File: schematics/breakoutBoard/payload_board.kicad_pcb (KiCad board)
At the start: 4 copper layers, 75 x 107 mm, 23 parts, among them P1 CONN_02X50, P2 CONN_02X50, P3 CONN_02X50, P4 CONN_02X50, U1 CBP, U2 TAMP, U3 CBP, U4 TAMP, U5 LAT-3, U6 TAMP

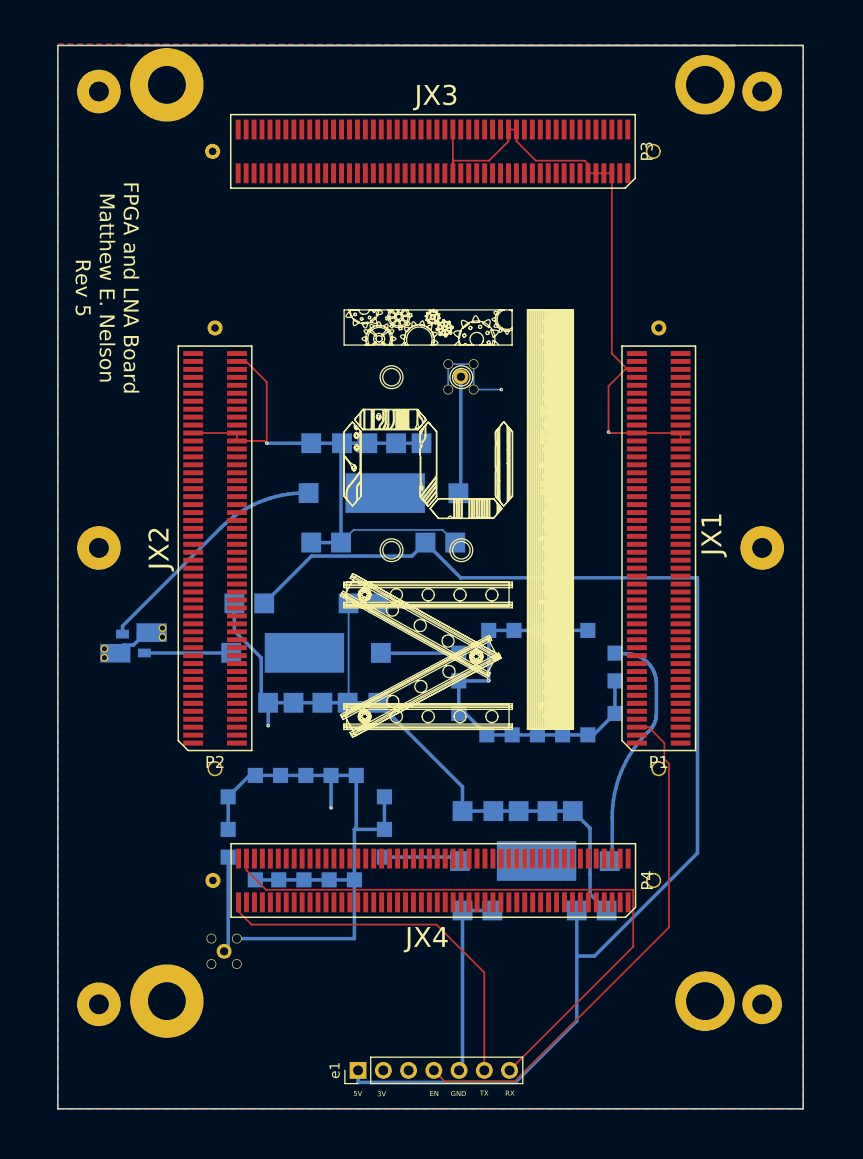
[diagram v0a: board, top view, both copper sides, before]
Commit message: Updated board to KiCad 6, pushing previous changes made.
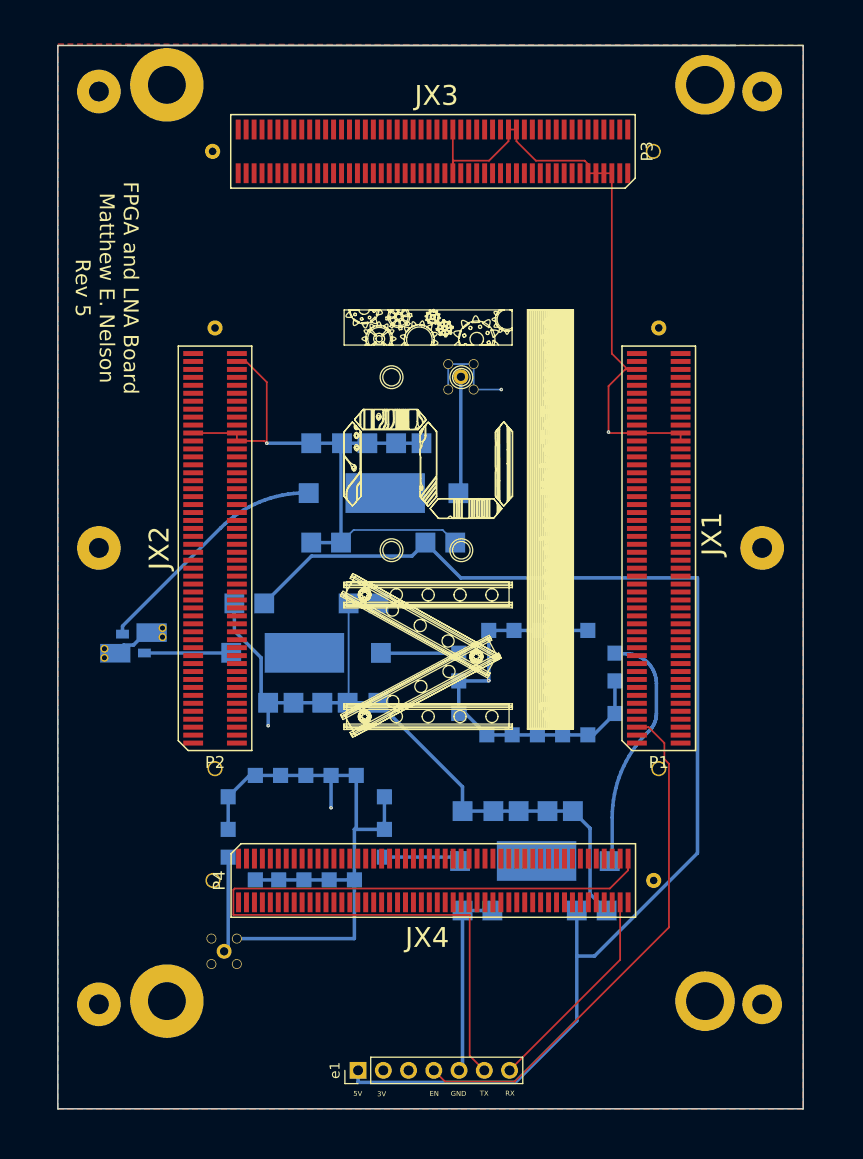
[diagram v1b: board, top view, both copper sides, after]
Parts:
- turned P4 to 0 degrees
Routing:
- net TX: track 38.0 -> 84.3 mm
- net RX: track 64.2 -> 21.5 mm
- net Net-(U5-Pad2): track 25.8 -> 24.8 mm
- net GND: track 218.7 -> 217.7 mm
- net Net-(U2-Pad5): track 25.7 -> 25.0 mm
- net RF_SIG: track 10.3 -> 9.65 mm
- added copper zone on In1.Cu, net GND
- added copper zone on In2.Cu, net RFGND
- removed copper zone on PGND, net GND
- removed copper zone on RFGND, net RFGND
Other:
- net class Default removed

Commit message: Update
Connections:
- net RF_SIG renamed /LNA Side/RF_SIG
- P1 pad 1: (no net) -> unconnected-(P1-Pad1)
- P1 pad 10: (no net) -> unconnected-(P1-Pad10)
- P1 pad 100: (no net) -> unconnected-(P1-Pad100)
- P1 pad 11: (no net) -> unconnected-(P1-Pad11)
- P1 pad 12: (no net) -> unconnected-(P1-Pad12)
- P1 pad 13: (no net) -> unconnected-(P1-Pad13)
- P1 pad 14: (no net) -> unconnected-(P1-Pad14)
- P1 pad 15: (no net) -> GND
- P1 pad 16: (no net) -> GND
- P1 pad 17: (no net) -> unconnected-(P1-Pad17)
- P1 pad 18: (no net) -> unconnected-(P1-Pad18)
- P1 pad 19: (no net) -> unconnected-(P1-Pad19)
- P1 pad 2: (no net) -> unconnected-(P1-Pad2)
- P1 pad 20: (no net) -> unconnected-(P1-Pad20)
- P1 pad 21: (no net) -> GND
- P1 pad 22: (no net) -> GND
- P1 pad 23: (no net) -> unconnected-(P1-Pad23)
- P1 pad 24: (no net) -> unconnected-(P1-Pad24)
- P1 pad 25: (no net) -> unconnected-(P1-Pad25)
- P1 pad 26: (no net) -> unconnected-(P1-Pad26)
- P1 pad 27: (no net) -> GND
- P1 pad 28: (no net) -> GND
- P1 pad 29: (no net) -> unconnected-(P1-Pad29)
- P1 pad 3: (no net) -> unconnected-(P1-Pad3)
- P1 pad 30: (no net) -> unconnected-(P1-Pad30)
- P1 pad 31: (no net) -> unconnected-(P1-Pad31)
- P1 pad 32: (no net) -> unconnected-(P1-Pad32)
- P1 pad 33: (no net) -> GND
- P1 pad 34: (no net) -> GND
- P1 pad 35: (no net) -> unconnected-(P1-Pad35)
- P1 pad 36: (no net) -> unconnected-(P1-Pad36)
- P1 pad 37: (no net) -> unconnected-(P1-Pad37)
- P1 pad 38: (no net) -> unconnected-(P1-Pad38)
- P1 pad 39: (no net) -> GND
- P1 pad 4: (no net) -> unconnected-(P1-Pad4)
- P1 pad 40: (no net) -> GND
- P1 pad 41: (no net) -> unconnected-(P1-Pad41)
- P1 pad 42: (no net) -> unconnected-(P1-Pad42)
- P1 pad 43: (no net) -> unconnected-(P1-Pad43)
- P1 pad 44: (no net) -> unconnected-(P1-Pad44)
- P1 pad 45: (no net) -> GND
- P1 pad 46: (no net) -> GND
- P1 pad 47: (no net) -> unconnected-(P1-Pad47)
- P1 pad 48: (no net) -> unconnected-(P1-Pad48)
- P1 pad 49: (no net) -> unconnected-(P1-Pad49)
- P1 pad 50: (no net) -> unconnected-(P1-Pad50)
- P1 pad 51: (no net) -> GND
- P1 pad 52: (no net) -> GND
- P1 pad 53: (no net) -> unconnected-(P1-Pad53)
- P1 pad 54: (no net) -> unconnected-(P1-Pad54)
- P1 pad 55: (no net) -> unconnected-(P1-Pad55)
- P1 pad 56: (no net) -> unconnected-(P1-Pad56)
- P1 pad 57: 3V -> 5V
- P1 pad 58: 3V -> 5V
- P1 pad 59: 3V -> 5V
- P1 pad 6: (no net) -> unconnected-(P1-Pad6)
- P1 pad 60: 3V -> 5V
- P1 pad 61: (no net) -> unconnected-(P1-Pad61)
- P1 pad 62: (no net) -> unconnected-(P1-Pad62)
- P1 pad 63: (no net) -> unconnected-(P1-Pad63)
- P1 pad 64: (no net) -> unconnected-(P1-Pad64)
- P1 pad 65: (no net) -> GND
- P1 pad 66: (no net) -> GND
- P1 pad 67: (no net) -> unconnected-(P1-Pad67)
- P1 pad 68: (no net) -> unconnected-(P1-Pad68)
- P1 pad 69: (no net) -> unconnected-(P1-Pad69)
- P1 pad 7: (no net) -> GND
- P1 pad 70: (no net) -> unconnected-(P1-Pad70)
- P1 pad 71: (no net) -> GND
- P1 pad 72: (no net) -> GND
- P1 pad 73: (no net) -> unconnected-(P1-Pad73)
- P1 pad 74: (no net) -> unconnected-(P1-Pad74)
- P1 pad 75: (no net) -> unconnected-(P1-Pad75)
- P1 pad 76: (no net) -> unconnected-(P1-Pad76)
- P1 pad 77: (no net) -> GND
- P1 pad 8: (no net) -> unconnected-(P1-Pad8)
- P1 pad 81: (no net) -> unconnected-(P1-Pad81)
- P1 pad 82: (no net) -> unconnected-(P1-Pad82)
- P1 pad 83: (no net) -> unconnected-(P1-Pad83)
- P1 pad 84: (no net) -> unconnected-(P1-Pad84)
- P1 pad 85: (no net) -> GND
- P1 pad 86: (no net) -> GND
- P1 pad 87: (no net) -> unconnected-(P1-Pad87)
- P1 pad 88: (no net) -> unconnected-(P1-Pad88)
- P1 pad 89: (no net) -> unconnected-(P1-Pad89)
- P1 pad 9: (no net) -> unconnected-(P1-Pad9)
- P1 pad 90: (no net) -> unconnected-(P1-Pad90)
- P1 pad 91: (no net) -> unconnected-(P1-Pad91)
- P1 pad 92: (no net) -> unconnected-(P1-Pad92)
- P1 pad 93: (no net) -> unconnected-(P1-Pad93)
- P1 pad 94: (no net) -> unconnected-(P1-Pad94)
- P1 pad 96: (no net) -> GND
- P1 pad 97: (no net) -> unconnected-(P1-Pad97)
- P1 pad 98: (no net) -> unconnected-(P1-Pad98)
- P1 pad 99: (no net) -> unconnected-(P1-Pad99)
- P2 pad 1: (no net) -> unconnected-(P2-Pad1)
- P2 pad 10: (no net) -> unconnected-(P2-Pad10)
- P2 pad 100: (no net) -> unconnected-(P2-Pad100)
- P2 pad 11: (no net) -> unconnected-(P2-Pad11)
- P2 pad 12: 3V -> 5V
- P2 pad 13: (no net) -> unconnected-(P2-Pad13)
- P2 pad 14: (no net) -> unconnected-(P2-Pad14)
- P2 pad 15: (no net) -> GND
- P2 pad 16: (no net) -> GND
- P2 pad 17: (no net) -> unconnected-(P2-Pad17)
- P2 pad 18: (no net) -> unconnected-(P2-Pad18)
- P2 pad 19: (no net) -> unconnected-(P2-Pad19)
- P2 pad 2: (no net) -> unconnected-(P2-Pad2)
- P2 pad 20: (no net) -> unconnected-(P2-Pad20)
- P2 pad 21: (no net) -> GND
- P2 pad 22: (no net) -> GND
- P2 pad 23: (no net) -> unconnected-(P2-Pad23)
- P2 pad 24: (no net) -> unconnected-(P2-Pad24)
- P2 pad 25: (no net) -> unconnected-(P2-Pad25)
- P2 pad 26: (no net) -> unconnected-(P2-Pad26)
- P2 pad 27: (no net) -> GND
- P2 pad 28: (no net) -> GND
- P2 pad 29: (no net) -> unconnected-(P2-Pad29)
- P2 pad 3: (no net) -> unconnected-(P2-Pad3)
- P2 pad 30: (no net) -> unconnected-(P2-Pad30)
- P2 pad 31: (no net) -> unconnected-(P2-Pad31)
- P2 pad 32: (no net) -> unconnected-(P2-Pad32)
- P2 pad 33: (no net) -> GND
- P2 pad 34: (no net) -> GND
- P2 pad 35: (no net) -> unconnected-(P2-Pad35)
- P2 pad 36: (no net) -> unconnected-(P2-Pad36)
- P2 pad 37: (no net) -> unconnected-(P2-Pad37)
- P2 pad 38: (no net) -> unconnected-(P2-Pad38)
- P2 pad 39: (no net) -> GND
- P2 pad 4: (no net) -> unconnected-(P2-Pad4)
- P2 pad 40: (no net) -> GND
- P2 pad 41: (no net) -> unconnected-(P2-Pad41)
- P2 pad 42: (no net) -> unconnected-(P2-Pad42)
- P2 pad 43: (no net) -> unconnected-(P2-Pad43)
- P2 pad 44: (no net) -> unconnected-(P2-Pad44)
- P2 pad 45: (no net) -> GND
- P2 pad 46: (no net) -> GND
- P2 pad 47: (no net) -> unconnected-(P2-Pad47)
- P2 pad 48: (no net) -> unconnected-(P2-Pad48)
- P2 pad 49: (no net) -> unconnected-(P2-Pad49)
- P2 pad 5: (no net) -> unconnected-(P2-Pad5)
- P2 pad 50: (no net) -> unconnected-(P2-Pad50)
- P2 pad 51: (no net) -> GND
- P2 pad 52: (no net) -> GND
- P2 pad 53: (no net) -> unconnected-(P2-Pad53)
- P2 pad 54: (no net) -> unconnected-(P2-Pad54)
- P2 pad 55: (no net) -> unconnected-(P2-Pad55)
- P2 pad 56: (no net) -> unconnected-(P2-Pad56)
- P2 pad 57: 3V -> 5V
- P2 pad 58: 3V -> 5V
- P2 pad 59: 3V -> 5V
- P2 pad 6: (no net) -> unconnected-(P2-Pad6)
- P2 pad 60: 3V -> 5V
- P2 pad 61: (no net) -> unconnected-(P2-Pad61)
- P2 pad 62: (no net) -> unconnected-(P2-Pad62)
- P2 pad 63: (no net) -> unconnected-(P2-Pad63)
- P2 pad 64: (no net) -> unconnected-(P2-Pad64)
- P2 pad 65: (no net) -> GND
- P2 pad 66: (no net) -> GND
- P2 pad 67: (no net) -> unconnected-(P2-Pad67)
- P2 pad 68: (no net) -> unconnected-(P2-Pad68)
- P2 pad 69: (no net) -> unconnected-(P2-Pad69)
- P2 pad 7: (no net) -> unconnected-(P2-Pad7)
- P2 pad 70: (no net) -> unconnected-(P2-Pad70)
- P2 pad 71: (no net) -> GND
- P2 pad 72: (no net) -> GND
- P2 pad 73: (no net) -> unconnected-(P2-Pad73)
- P2 pad 74: (no net) -> unconnected-(P2-Pad74)
- P2 pad 75: (no net) -> unconnected-(P2-Pad75)
- P2 pad 76: (no net) -> unconnected-(P2-Pad76)
- P2 pad 77: (no net) -> GND
- P2 pad 8: (no net) -> unconnected-(P2-Pad8)
- P2 pad 81: (no net) -> unconnected-(P2-Pad81)
- P2 pad 82: (no net) -> unconnected-(P2-Pad82)
- P2 pad 83: (no net) -> unconnected-(P2-Pad83)
- P2 pad 84: (no net) -> unconnected-(P2-Pad84)
- P2 pad 85: (no net) -> GND
- P2 pad 86: (no net) -> GND
- P2 pad 87: (no net) -> unconnected-(P2-Pad87)
- P2 pad 88: (no net) -> unconnected-(P2-Pad88)
- P2 pad 89: (no net) -> unconnected-(P2-Pad89)
- P2 pad 9: (no net) -> unconnected-(P2-Pad9)
- P2 pad 90: (no net) -> unconnected-(P2-Pad90)
- P2 pad 91: (no net) -> unconnected-(P2-Pad91)
- P2 pad 92: (no net) -> unconnected-(P2-Pad92)
- P2 pad 93: (no net) -> unconnected-(P2-Pad93)
- P2 pad 94: (no net) -> unconnected-(P2-Pad94)
- P2 pad 95: (no net) -> GND
- P2 pad 96: (no net) -> GND
- P2 pad 97: (no net) -> unconnected-(P2-Pad97)
- P2 pad 99: (no net) -> unconnected-(P2-Pad99)
- P3 pad 1: (no net) -> unconnected-(P3-Pad1)
- P3 pad 10: (no net) -> unconnected-(P3-Pad10)
- P3 pad 100: (no net) -> unconnected-(P3-Pad100)
- P3 pad 12: (no net) -> GND
- P3 pad 13: (no net) -> unconnected-(P3-Pad13)
- P3 pad 14: (no net) -> unconnected-(P3-Pad14)
- P3 pad 15: (no net) -> unconnected-(P3-Pad15)
- P3 pad 16: (no net) -> unconnected-(P3-Pad16)
- P3 pad 17: (no net) -> GND
- P3 pad 18: (no net) -> unconnected-(P3-Pad18)
- P3 pad 19: (no net) -> unconnected-(P3-Pad19)
- P3 pad 2: (no net) -> unconnected-(P3-Pad2)
- P3 pad 20: (no net) -> unconnected-(P3-Pad20)
- P3 pad 21: (no net) -> unconnected-(P3-Pad21)
- P3 pad 22: (no net) -> unconnected-(P3-Pad22)
- P3 pad 23: (no net) -> GND
- P3 pad 24: (no net) -> GND
- P3 pad 25: (no net) -> unconnected-(P3-Pad25)
- P3 pad 26: (no net) -> unconnected-(P3-Pad26)
- P3 pad 27: (no net) -> unconnected-(P3-Pad27)
- P3 pad 28: (no net) -> unconnected-(P3-Pad28)
- P3 pad 29: (no net) -> GND
- P3 pad 3: (no net) -> unconnected-(P3-Pad3)
- P3 pad 31: (no net) -> unconnected-(P3-Pad31)
- P3 pad 33: (no net) -> unconnected-(P3-Pad33)
- P3 pad 34: (no net) -> unconnected-(P3-Pad34)
- P3 pad 35: (no net) -> GND
- P3 pad 36: (no net) -> GND
- P3 pad 37: (no net) -> unconnected-(P3-Pad37)
- P3 pad 38: (no net) -> unconnected-(P3-Pad38)
- P3 pad 39: (no net) -> unconnected-(P3-Pad39)
- P3 pad 4: (no net) -> unconnected-(P3-Pad4)
- P3 pad 40: (no net) -> GND
- P3 pad 41: (no net) -> unconnected-(P3-Pad41)
- P3 pad 42: (no net) -> unconnected-(P3-Pad42)
- P3 pad 43: (no net) -> unconnected-(P3-Pad43)
- P3 pad 44: (no net) -> unconnected-(P3-Pad44)
- P3 pad 47: (no net) -> unconnected-(P3-Pad47)
- P3 pad 48: (no net) -> unconnected-(P3-Pad48)
- P3 pad 49: (no net) -> GND
- P3 pad 50: (no net) -> GND
- P3 pad 51: (no net) -> unconnected-(P3-Pad51)
- P3 pad 52: (no net) -> unconnected-(P3-Pad52)
- P3 pad 53: (no net) -> unconnected-(P3-Pad53)
- P3 pad 54: (no net) -> unconnected-(P3-Pad54)
- P3 pad 55: (no net) -> GND
- P3 pad 56: (no net) -> GND
- P3 pad 57: (no net) -> unconnected-(P3-Pad57)
- P3 pad 58: (no net) -> unconnected-(P3-Pad58)
- P3 pad 59: (no net) -> unconnected-(P3-Pad59)
- P3 pad 6: (no net) -> GND
- P3 pad 60: (no net) -> unconnected-(P3-Pad60)
- P3 pad 61: (no net) -> GND
- P3 pad 62: (no net) -> GND
- P3 pad 63: (no net) -> unconnected-(P3-Pad63)
- P3 pad 64: (no net) -> unconnected-(P3-Pad64)
- P3 pad 65: (no net) -> GND
- P3 pad 66: (no net) -> unconnected-(P3-Pad66)
- P3 pad 67: (no net) -> unconnected-(P3-Pad67)
- P3 pad 68: (no net) -> unconnected-(P3-Pad68)
- P3 pad 69: (no net) -> unconnected-(P3-Pad69)
- P3 pad 70: (no net) -> unconnected-(P3-Pad70)
- P3 pad 71: (no net) -> GND
- P3 pad 72: (no net) -> GND
- P3 pad 73: (no net) -> unconnected-(P3-Pad73)
- P3 pad 74: (no net) -> unconnected-(P3-Pad74)
- P3 pad 75: (no net) -> unconnected-(P3-Pad75)
- P3 pad 76: (no net) -> unconnected-(P3-Pad76)
- P3 pad 77: (no net) -> GND
- P3 pad 78: (no net) -> GND
- P3 pad 79: (no net) -> unconnected-(P3-Pad79)
- P3 pad 8: (no net) -> unconnected-(P3-Pad8)
- P3 pad 80: (no net) -> unconnected-(P3-Pad80)
- P3 pad 81: (no net) -> unconnected-(P3-Pad81)
- P3 pad 82: (no net) -> unconnected-(P3-Pad82)
- P3 pad 83: (no net) -> GND
- P3 pad 84: (no net) -> GND
- P3 pad 85: (no net) -> unconnected-(P3-Pad85)
- P3 pad 86: (no net) -> unconnected-(P3-Pad86)
- P3 pad 87: (no net) -> unconnected-(P3-Pad87)
- P3 pad 88: (no net) -> unconnected-(P3-Pad88)
- P3 pad 89: (no net) -> unconnected-(P3-Pad89)
- P3 pad 90: (no net) -> unconnected-(P3-Pad90)
- P3 pad 91: (no net) -> unconnected-(P3-Pad91)
- P3 pad 92: (no net) -> unconnected-(P3-Pad92)
- P3 pad 93: (no net) -> unconnected-(P3-Pad93)
- P3 pad 94: (no net) -> unconnected-(P3-Pad94)
- P3 pad 95: (no net) -> GND
- P3 pad 96: (no net) -> GND
- P3 pad 97: (no net) -> unconnected-(P3-Pad97)
- P3 pad 98: (no net) -> unconnected-(P3-Pad98)
- P3 pad 99: (no net) -> unconnected-(P3-Pad99)
- P4 pad 1: (no net) -> unconnected-(P4-Pad1)
- P4 pad 10: (no net) -> unconnected-(P4-Pad10)
- P4 pad 100: (no net) -> unconnected-(P4-Pad100)
- P4 pad 11: (no net) -> GND
- P4 pad 12: (no net) -> GND
- P4 pad 13: (no net) -> unconnected-(P4-Pad13)
- P4 pad 14: (no net) -> unconnected-(P4-Pad14)
- P4 pad 15: (no net) -> unconnected-(P4-Pad15)
- P4 pad 16: (no net) -> unconnected-(P4-Pad16)
- P4 pad 17: (no net) -> GND
- P4 pad 18: (no net) -> GND
- P4 pad 19: (no net) -> unconnected-(P4-Pad19)
- P4 pad 2: (no net) -> unconnected-(P4-Pad2)
- P4 pad 20: (no net) -> unconnected-(P4-Pad20)
- P4 pad 21: (no net) -> unconnected-(P4-Pad21)
- P4 pad 22: (no net) -> unconnected-(P4-Pad22)
- P4 pad 23: (no net) -> GND
- P4 pad 24: (no net) -> GND
- P4 pad 25: (no net) -> unconnected-(P4-Pad25)
- P4 pad 26: (no net) -> unconnected-(P4-Pad26)
- P4 pad 27: (no net) -> unconnected-(P4-Pad27)
- P4 pad 28: (no net) -> unconnected-(P4-Pad28)
- P4 pad 29: (no net) -> GND
- P4 pad 3: (no net) -> unconnected-(P4-Pad3)
- P4 pad 30: (no net) -> GND
- P4 pad 31: (no net) -> unconnected-(P4-Pad31)
- P4 pad 32: (no net) -> unconnected-(P4-Pad32)
- P4 pad 33: (no net) -> unconnected-(P4-Pad33)
- P4 pad 34: (no net) -> unconnected-(P4-Pad34)
- P4 pad 35: (no net) -> unconnected-(P4-Pad35)
- P4 pad 36: (no net) -> unconnected-(P4-Pad36)
- P4 pad 37: (no net) -> unconnected-(P4-Pad37)
- P4 pad 38: (no net) -> unconnected-(P4-Pad38)
- P4 pad 39: (no net) -> GND
- P4 pad 4: (no net) -> unconnected-(P4-Pad4)
- P4 pad 40: (no net) -> GND
- P4 pad 41: (no net) -> unconnected-(P4-Pad41)
- P4 pad 42: (no net) -> unconnected-(P4-Pad42)
- P4 pad 43: (no net) -> unconnected-(P4-Pad43)
- P4 pad 44: (no net) -> unconnected-(P4-Pad44)
- P4 pad 45: (no net) -> unconnected-(P4-Pad45)
- P4 pad 46: (no net) -> unconnected-(P4-Pad46)
- P4 pad 47: (no net) -> unconnected-(P4-Pad47)
- P4 pad 48: (no net) -> unconnected-(P4-Pad48)
- P4 pad 49: (no net) -> GND
- P4 pad 5: (no net) -> GND
- P4 pad 50: (no net) -> GND
- P4 pad 51: (no net) -> unconnected-(P4-Pad51)
- P4 pad 52: (no net) -> unconnected-(P4-Pad52)
- P4 pad 53: (no net) -> unconnected-(P4-Pad53)
- P4 pad 54: (no net) -> unconnected-(P4-Pad54)
- P4 pad 55: (no net) -> GND
- P4 pad 56: (no net) -> GND
- P4 pad 57: (no net) -> unconnected-(P4-Pad57)
- P4 pad 58: (no net) -> unconnected-(P4-Pad58)
- P4 pad 59: (no net) -> unconnected-(P4-Pad59)
- P4 pad 6: (no net) -> GND
- P4 pad 60: (no net) -> unconnected-(P4-Pad60)
- P4 pad 61: (no net) -> GND
- P4 pad 62: (no net) -> GND
- P4 pad 63: (no net) -> unconnected-(P4-Pad63)
- P4 pad 64: (no net) -> unconnected-(P4-Pad64)
- P4 pad 65: (no net) -> GND
- P4 pad 66: (no net) -> GND
- P4 pad 67: (no net) -> unconnected-(P4-Pad67)
- P4 pad 68: (no net) -> unconnected-(P4-Pad68)
- P4 pad 69: (no net) -> unconnected-(P4-Pad69)
- P4 pad 7: (no net) -> unconnected-(P4-Pad7)
- P4 pad 70: (no net) -> unconnected-(P4-Pad70)
- P4 pad 71: (no net) -> GND
- P4 pad 72: (no net) -> GND
- P4 pad 73: (no net) -> unconnected-(P4-Pad73)
- P4 pad 74: (no net) -> unconnected-(P4-Pad74)
- P4 pad 75: (no net) -> unconnected-(P4-Pad75)
- P4 pad 76: (no net) -> unconnected-(P4-Pad76)
- P4 pad 77: (no net) -> unconnected-(P4-Pad77)
- P4 pad 78: (no net) -> unconnected-(P4-Pad78)
- P4 pad 79: (no net) -> unconnected-(P4-Pad79)
- P4 pad 8: (no net) -> unconnected-(P4-Pad8)
- P4 pad 80: (no net) -> unconnected-(P4-Pad80)
- P4 pad 81: (no net) -> unconnected-(P4-Pad81)
- P4 pad 82: (no net) -> unconnected-(P4-Pad82)
- P4 pad 83: (no net) -> GND
- P4 pad 84: (no net) -> GND
- P4 pad 85: (no net) -> unconnected-(P4-Pad85)
- P4 pad 86: (no net) -> unconnected-(P4-Pad86)
- P4 pad 87: (no net) -> unconnected-(P4-Pad87)
- P4 pad 88: (no net) -> unconnected-(P4-Pad88)
- P4 pad 89: (no net) -> GND
- P4 pad 9: (no net) -> unconnected-(P4-Pad9)
- P4 pad 90: (no net) -> GND
- P4 pad 91: (no net) -> unconnected-(P4-Pad91)
- P4 pad 92: (no net) -> unconnected-(P4-Pad92)
- P4 pad 93: (no net) -> unconnected-(P4-Pad93)
- P4 pad 94: (no net) -> unconnected-(P4-Pad94)
- P4 pad 95: (no net) -> GND
- P4 pad 96: (no net) -> GND
- P4 pad 97: (no net) -> unconnected-(P4-Pad97)
- P4 pad 98: RX -> TX
- P4 pad 99: TX -> RX
- U1 pad 15: RFGND -> Net-(U1-Pad15)
- U1 pad 7: RFGND -> Net-(U1-Pad15)
- U3 pad 15: RFGND -> Net-(U3-Pad15)
- U3 pad 7: RFGND -> Net-(U3-Pad15)
- e1 pad 2: 3V -> 5V
- e1 pad 3: (no net) -> RFGND
- e1 pad 6: TX -> RX
- e1 pad 7: RX -> TX
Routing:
- net GND: track 217.7 -> 842.2 mm, vias 3 -> 4
- net TX: track 84.3 -> 21.5 mm
- net RX: track 21.5 -> 80.1 mm
- net RFGND: track 121.5 -> 137.0 mm
- added copper zone on F.Cu, net 5V
- removed copper zone on F.Cu, net 3V

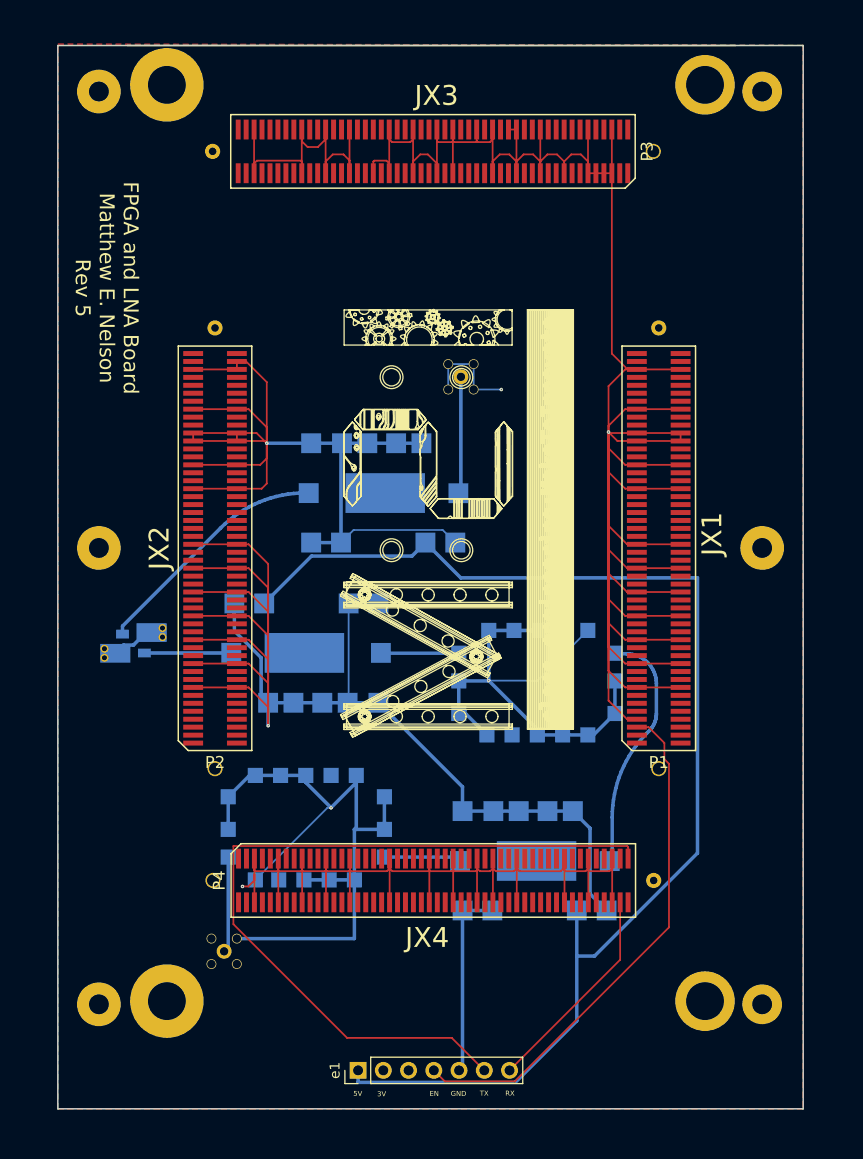
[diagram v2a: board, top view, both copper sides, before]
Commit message: Fixed grounding issue
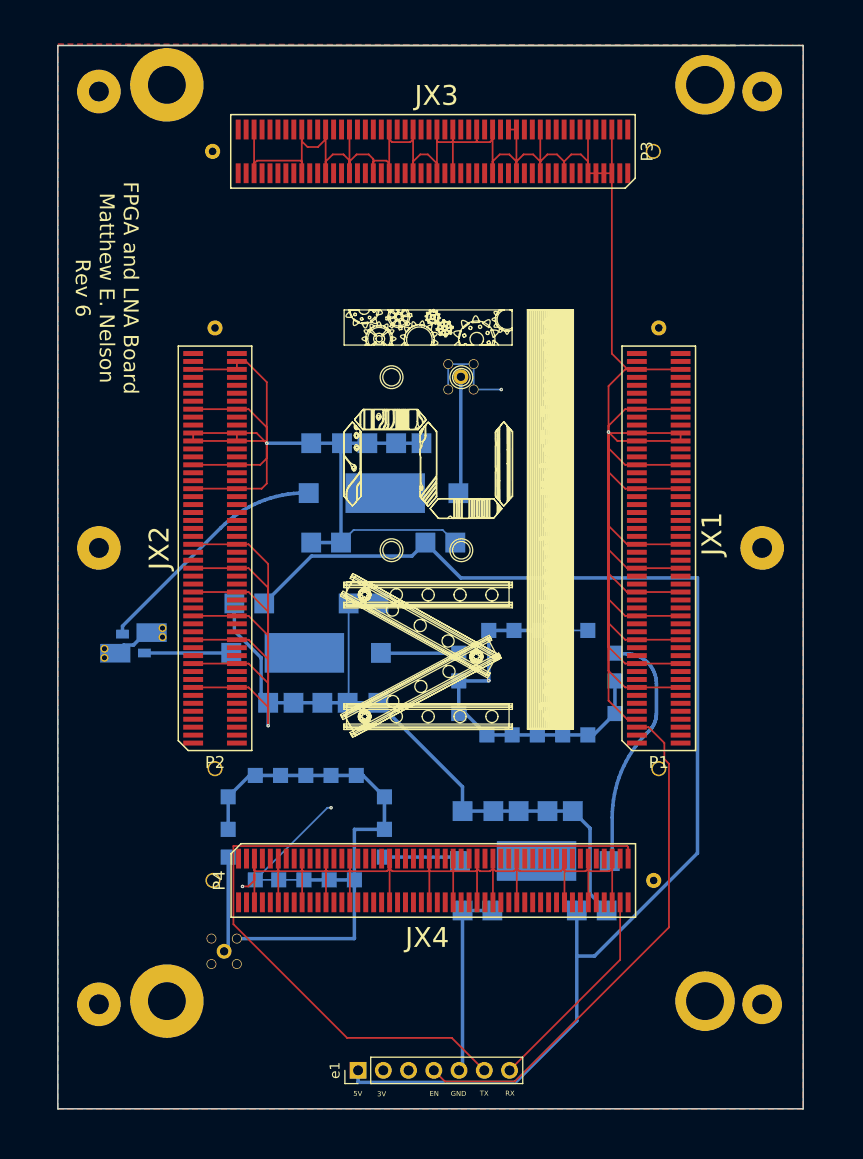
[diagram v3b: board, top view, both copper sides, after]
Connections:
- U1 pad 15: Net-(U1-Pad15) -> RFGND
- U1 pad 7: Net-(U1-Pad15) -> RFGND
- U2 pad 12: (no net) -> unconnected-(U2-Pad12)
- U3 pad 15: Net-(U3-Pad15) -> RFGND
- U3 pad 7: Net-(U3-Pad15) -> RFGND
- U4 pad 12: (no net) -> unconnected-(U4-Pad12)
- U6 pad 12: (no net) -> unconnected-(U6-Pad12)
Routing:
- net RFGND: track 137.0 -> 127.0 mm
- net GND: track 842.2 -> 847.7 mm
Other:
- board text added: "FPGA and LNA Board Matthew E. Nelson Rev 6"
- board text removed: "FPGA and LNA Board Matthew E. Nelson Rev 5"
